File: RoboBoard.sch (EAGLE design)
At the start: 31 parts, among them IC2 L293D

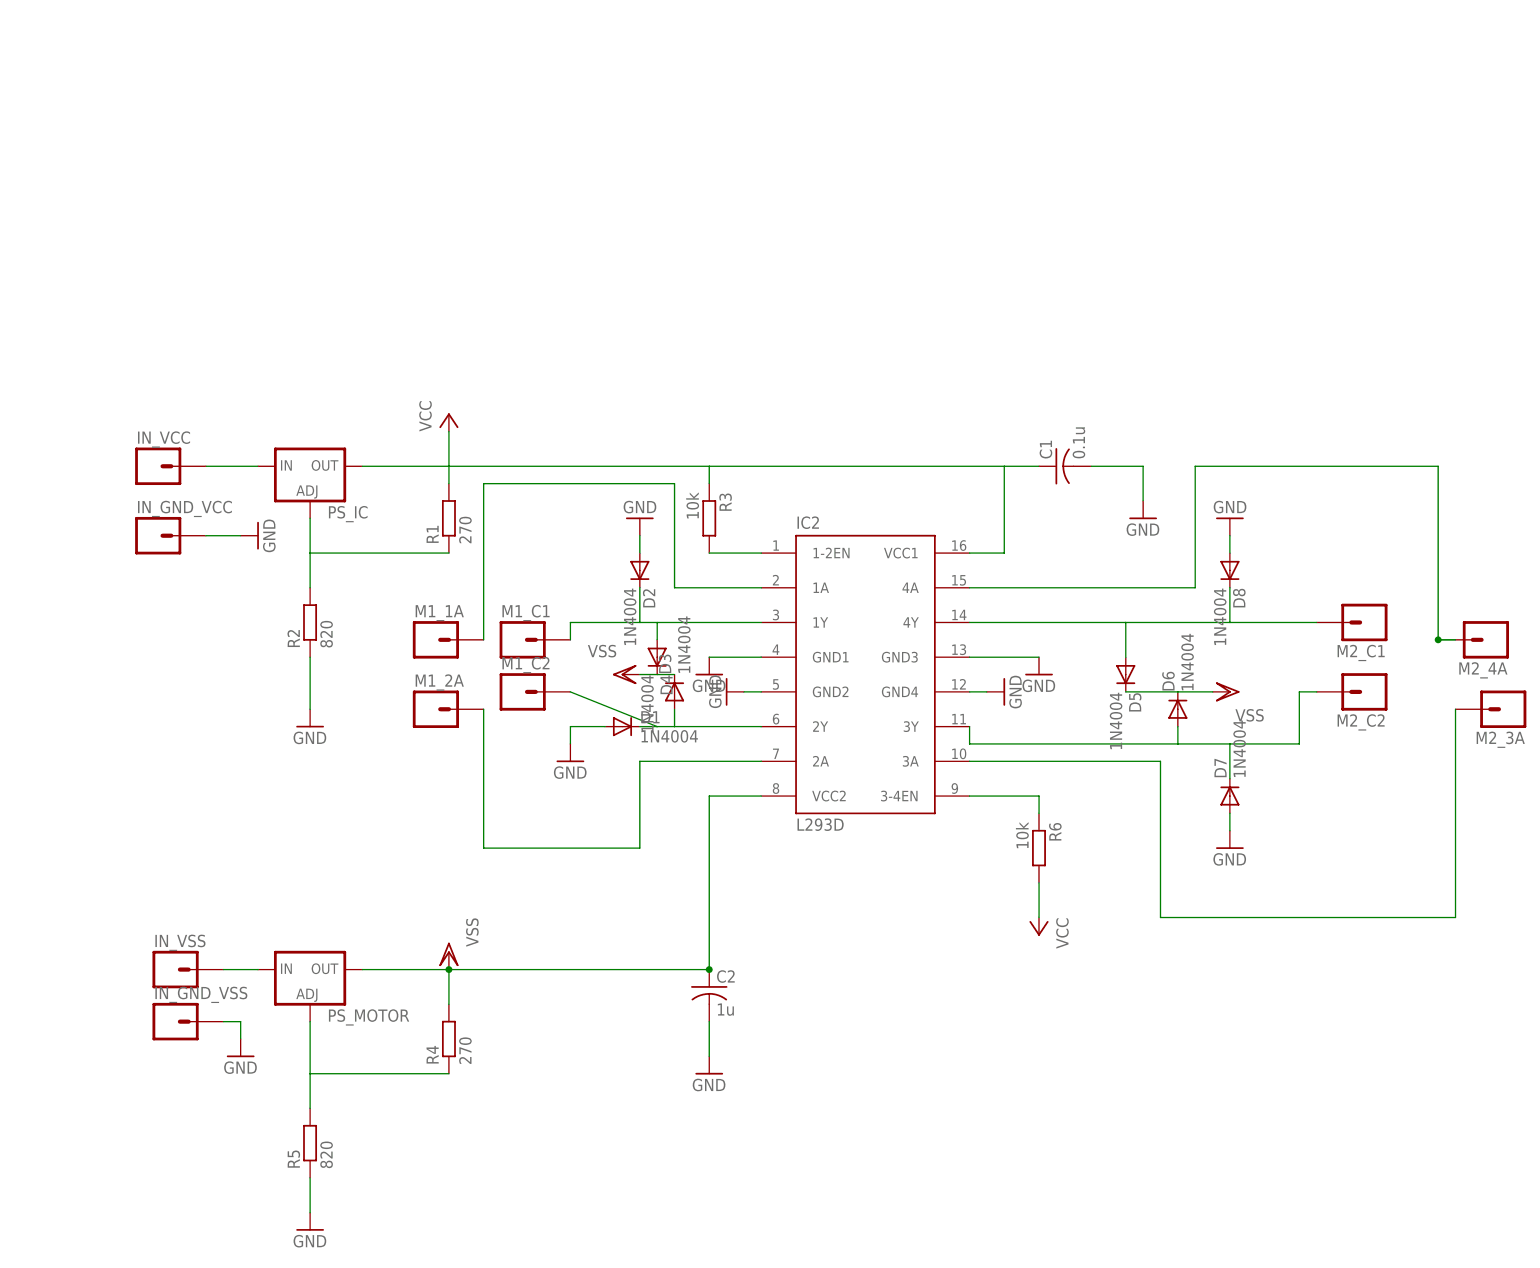
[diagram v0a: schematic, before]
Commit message: fix:	Fixing motor rotations
Fixin motor rotations to allow left and rights turns.
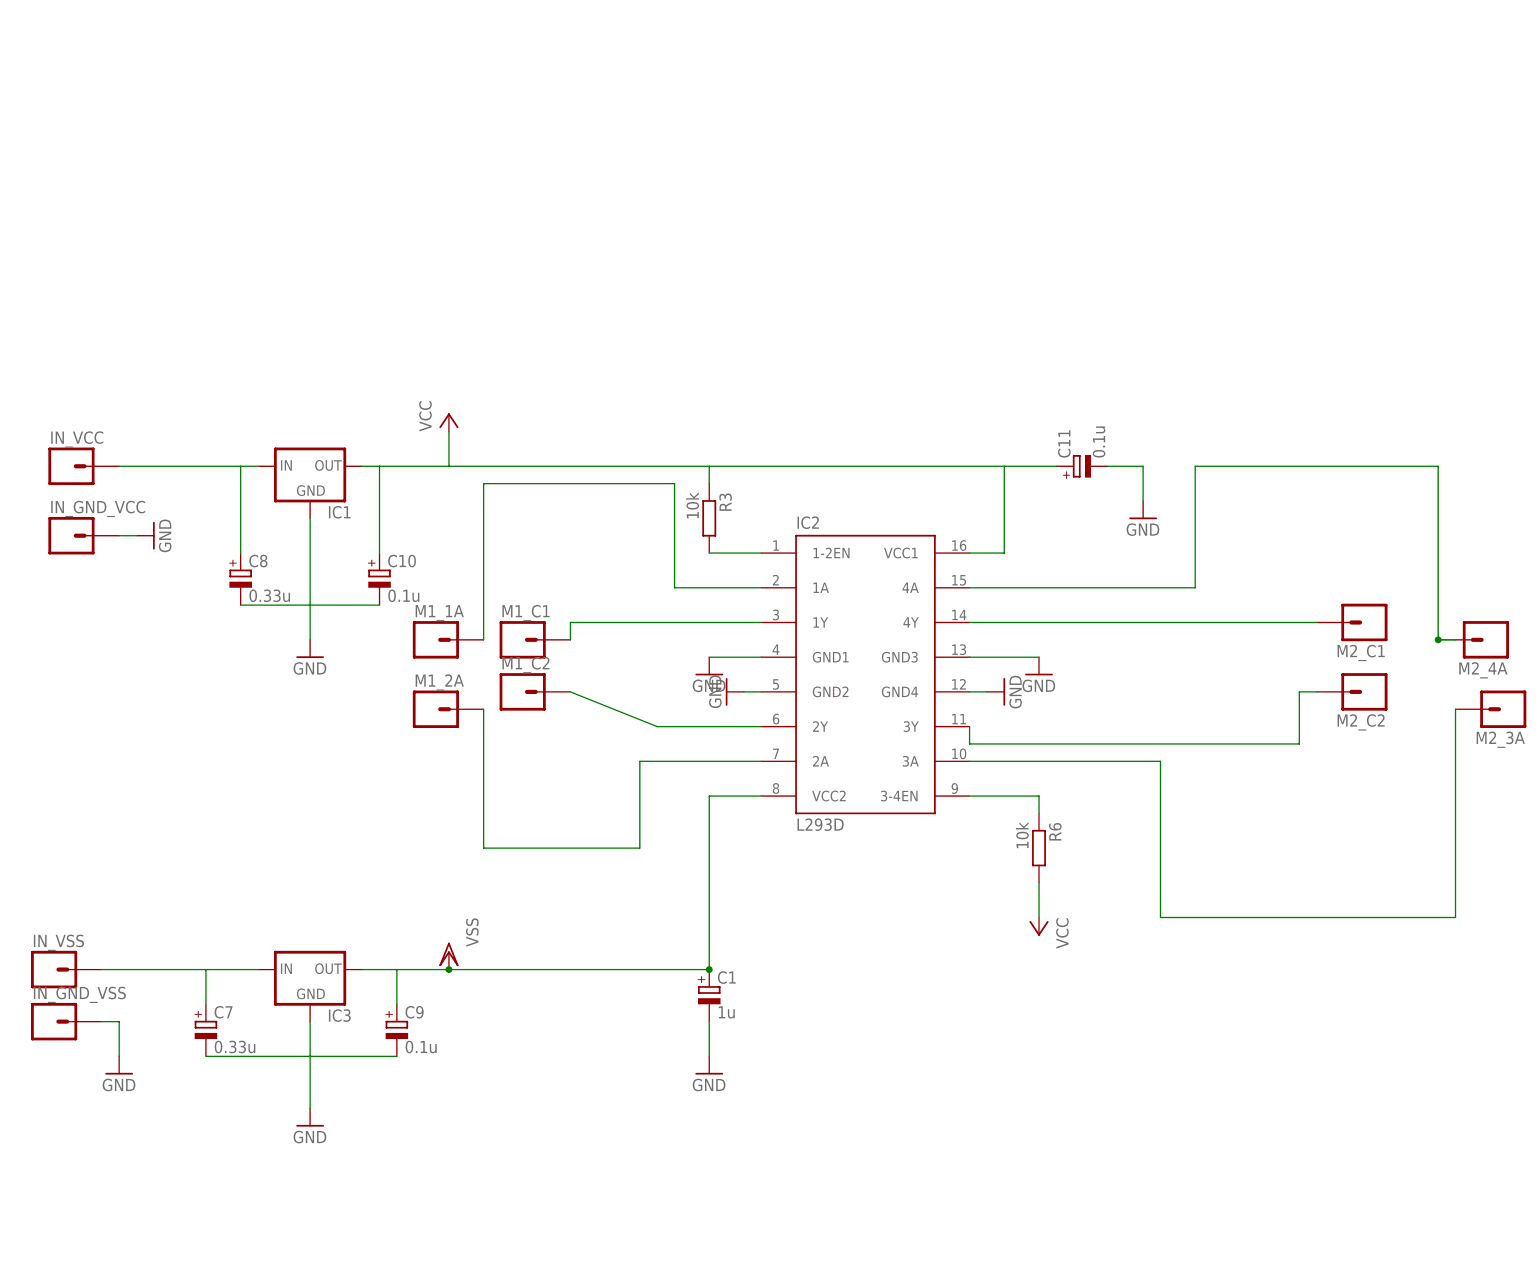
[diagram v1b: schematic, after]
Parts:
- removed C2: 1u, resistor:C-US025-030X050
- removed D1, D2, D3, D4, D5, D6, D7, D8: 1N4004, diode:1N4004
- removed PS_IC, PS_MOTOR: (no value), v-reg:LM317TL
- removed R1, R4: 270, resistor:R-EU_0204/7
- removed R2, R5: 820, resistor:R-EU_0204/7
- added C10, C11, C9: 0.1u, resistor:CPOL-EUE1.8-4
- added C7, C8: 0.33u, resistor:CPOL-EUE1.8-4
- added IC1, IC3: (no value), v-reg:78XXL
- C1: value 0.1u -> 1u; device resistor:C-US025-030X050 -> resistor:CPOL-EUE1.8-4
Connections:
- removed net N$2: PS_IC.ADJ, R1.1, R2.2
- removed net N$7: PS_MOTOR.ADJ, R4.1, R5.2
- net GND: now also C1.-, C10.-, C11.-, C7.-, C8.-, C9.-, IC1.GND, IC3.GND; no longer C1.2, C2.2, D1.A, D2.A, D7.A, D8.A, R2.1, R5.1
- net N$10: no longer D6.A, D7.C
- net N$3: no longer D2.C, D4.A
- net N$4: no longer D1.C, D3.A
- net N$5: now also C7.+, IC3.IN; no longer PS_MOTOR.IN
- net N$6: now also C8.+, IC1.IN; no longer PS_IC.IN
- net N$9: no longer D5.A, D8.C
- net VCC: now also C10.+, C11.+, IC1.OUT; no longer C1.1, PS_IC.OUT, R1.2
- net VSS: now also C1.+, C9.+, IC3.OUT; no longer C2.1, D3.C, D4.C, D5.C, D6.C, PS_MOTOR.OUT, R4.2
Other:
- moved on the sheet: IN_GND_VCC, IN_GND_VSS, IN_VCC, IN_VSS

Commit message: fix:	Fixing board layout
Fixing the board layout
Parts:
- removed C10, C9: 0.1u, resistor:CPOL-EUE1.8-4
- removed C7, C8: 0.33u, resistor:CPOL-EUE1.8-4
- removed IC1, IC3: (no value), v-reg:78XXL
- removed IN_GND_VCC, IN_GND_VSS, IN_VCC, IN_VSS, M1_1A, M1_2A, M1_C1, M1_C2, M2_3A, M2_4A, M2_C1, M2_C2: (no value), SparkFun-Connectors:M01PTH_LONGPAD
- removed R6: 10k, resistor:R-EU_0204/7
- added INVCC: (no value), SparkFun-Connectors:M02LOCK_LONGPADS
- added J1, J2: (no value), SparkFun-Connectors:M15LOCK_LONGPADS
- added RANGE1: (no value), SparkFun-Connectors:M04LONGPADS
- added RJ1, RJ2: (no value), rj11:RJ11
- added S2: (no value), adafruit:EG1218S
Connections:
- removed net N$11: IC2.1A, M1_1A.1
- removed net N$14: IC2.3A, M2_3A.1
- removed net VSS: C1.+, C9.+, IC2.VCC2, IC3.OUT
- new net N$2: IC2.2Y, RJ1.P$4
- new net N$7: IC2.3A, J1.7
- net GND: now also INVCC.2, J2.14, RANGE1.1; no longer C10.-, C7.-, C8.-, C9.-, IC1.GND, IC3.GND, IN_GND_VCC.1, IN_GND_VSS.1
- net N$1: now also IC2.1Y, RJ1.P$1; no longer IC2.1-2EN, R3.2
- net N$10: now also IC2.1A, J1.4; no longer IC2.3Y, M2_C2.1
- net N$12: now also J1.1, RANGE1.2; no longer IC2.2A, M1_2A.1
- net N$13: now also J2.15, S2.S; no longer IC2.4A, M2_4A.1
- net N$3: now also IC2.3Y, RJ2.P$1, RJ2.P$2; no longer IC2.1Y, M1_C1.1
- net N$4: now also IC2.4Y, RJ2.P$3, RJ2.P$4; no longer IC2.2Y, M1_C2.1
- net N$5: now also IC2.4A, J1.10; no longer C7.+, IC3.IN, IN_VSS.1
- net N$6: now also J2.1, RANGE1.3; no longer C8.+, IC1.IN, IN_VCC.1
- net N$8: now also IC2.1-2EN, R3.2; no longer R6.1
- net N$9: now also IC2.2A, J1.8; no longer IC2.4Y, M2_C1.1
- net VCC: now also C1.+, IC2.VCC2, INVCC.1, RANGE1.4, S2.P; no longer C10.+, IC1.OUT, R6.2
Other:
- moved on the sheet: C1
